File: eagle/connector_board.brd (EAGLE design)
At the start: 22.6 x 24.3 mm, 26 parts, among them IC1 MEGA8-MI, J1 FH12-6S-0.5SH(55), J2 FH12-6S-0.5SH(55), J3 FH12-6S-0.5SH(55), J4 FH12-6S-0.5SH(55), X4 POGOPIN-CONNWITHVIAS-SMV, X6 POGOPIN-CONNWITHVIAS-SMV

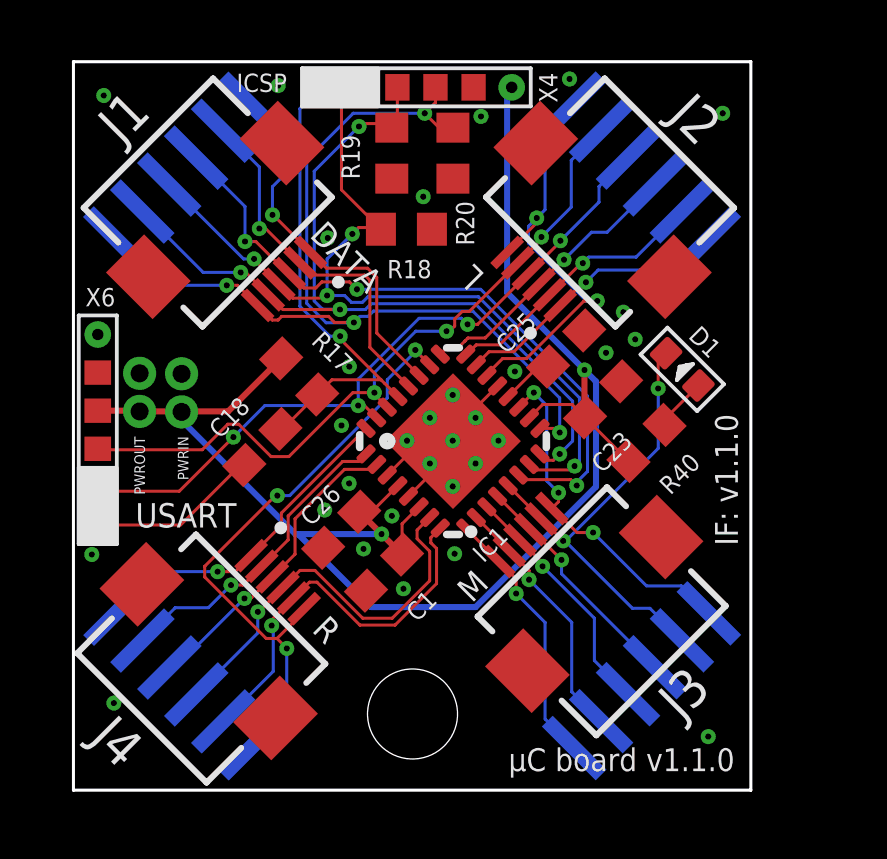
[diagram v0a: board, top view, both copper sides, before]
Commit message: Add pogoprog pads on both sides of board
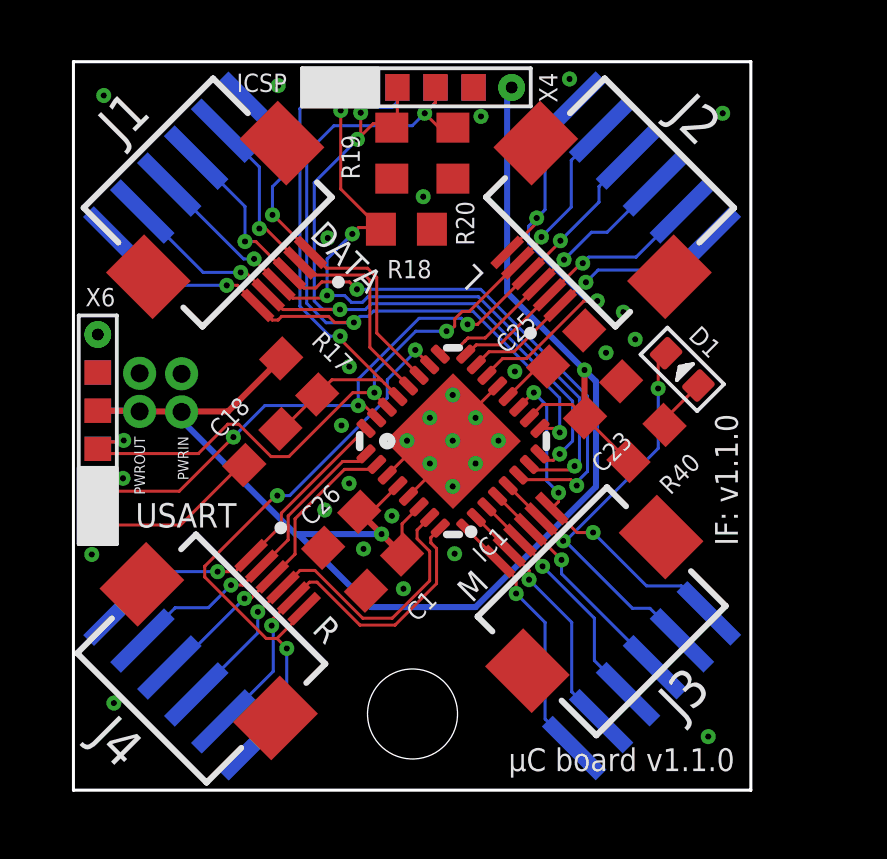
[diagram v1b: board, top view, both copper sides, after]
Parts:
- added X1, X2: POGOPIN-CONNWITHVIAS-SMV, Protofusion:POGOPROG-CONN-OH-SMALLERVIAS
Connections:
- net !RESET: now also X2.1
- net DTR: now also X1.1
- net GND: now also X1.5, X1.6, X2.5
- net MISO: now also X2.3
- net MOSI: now also X2.2
- net RXD: now also X1.3
- net SCK: now also X2.4
- net TXD: now also X1.2
- net VCC: now also X1.4, X2.6
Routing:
- net MISO: track 30.5 -> 33.1 mm, vias 4 -> 5
- net RXD: track 0.12 -> 2.35 mm, vias 0 -> 1
- net TXD: track 0.09 -> 2.10 mm, vias 0 -> 1
- net VCC: track 53.9 -> 55.3 mm
- net SCK: track 32.8 -> 33.9 mm
- net MOSI: track 29.8 -> 30.8 mm, vias 4 -> 5

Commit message: Make room for v-score on the edges by rotating connectors 45degs
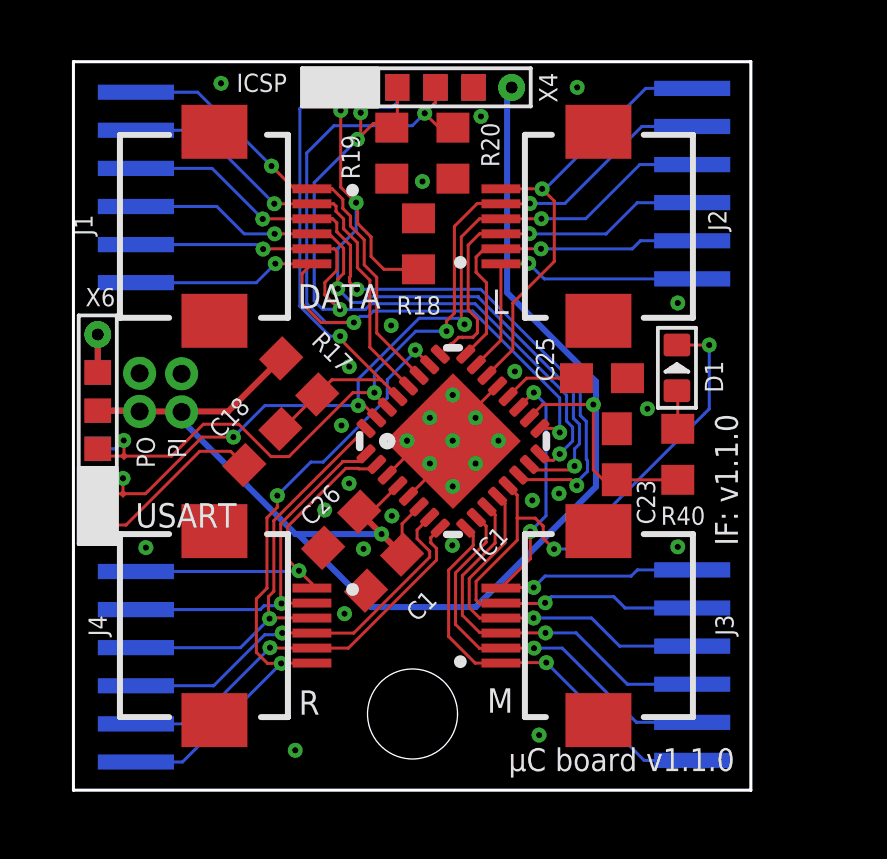
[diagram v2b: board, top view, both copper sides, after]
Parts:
- moved U$3 3.97 mm to (20.6, 23.4), turned to 270 degrees
- moved U$2 3.84 mm to (2.08, 0.94), turned to 90 degrees
- moved J3 3.13 mm to (14.2, 5.49), turned to 90 degrees
- moved J2 2.07 mm to (14.2, 18.8), turned to 90 degrees
- moved J1 1.98 mm to (7.95, 18.8), turned to 270 degrees
- moved C23 1.89 mm to (18.1, 11.2), turned to 90 degrees
- moved J4 1.84 mm to (7.95, 5.49), turned to 270 degrees
- moved U$4 1.63 mm to (2.08, 16.9), turned to 90 degrees
- moved C25 1.55 mm to (17.6, 13.7), turned to 0 degrees
- moved U$1 1.55 mm to (20.6, 7.34), turned to 270 degrees
- moved R40 1.11 mm to (20.1, 11.2), turned to 90 degrees
- moved SH1 0.80 mm to (1.68, 11.1)
- moved SH2 0.79 mm to (1.65, 9.88)
- moved R18 0.63 mm to (11.5, 18.2), turned to 90 degrees
- moved D1 0.18 mm to (20.1, 14.1), turned to 90 degrees
- renumbered PWRIN to PI, PWROUT to PO
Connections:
- net ENCR1A: now also IC1.2; no longer IC1.32
- net LEDR: now also IC1.32; no longer IC1.2
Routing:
- net ENCM2B: track 15.7 -> 24.2 mm, vias 2 -> 3
- net ENCM1A: track 8.83 -> 14.0 mm
- net LEDM: track 8.19 -> 13.1 mm
- net ENCM1B: track 8.51 -> 13.4 mm
- net ENCM2A: track 7.89 -> 12.3 mm
- net MOSI: track 30.8 -> 34.9 mm
- net LEDR: track 10.4 -> 14.0 mm
- net SWM: track 11.7 -> 15.0 mm
- net LEDL: track 9.50 -> 12.6 mm
- net ENCL2B: track 24.3 -> 27.4 mm
- net SDA: track 12.5 -> 15.3 mm
- net ENCL2A: track 24.0 -> 26.8 mm
- net GND: track 4.17 -> 6.71 mm
- net SCL: track 12.2 -> 14.7 mm
- net ENCL1B: track 9.13 -> 11.1 mm
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
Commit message: Fix connector board issues for manufacuring;
The minimum trace width and clearance allowed on a 1.6mm thick pcb is
6mils. For some reason 4mils was used when designing the board (maybe
JLCPCB design rules?).

Also some of the texts were on the wrong layers / places and would not
be printed on the board / would be printed on top of components / other
texts.
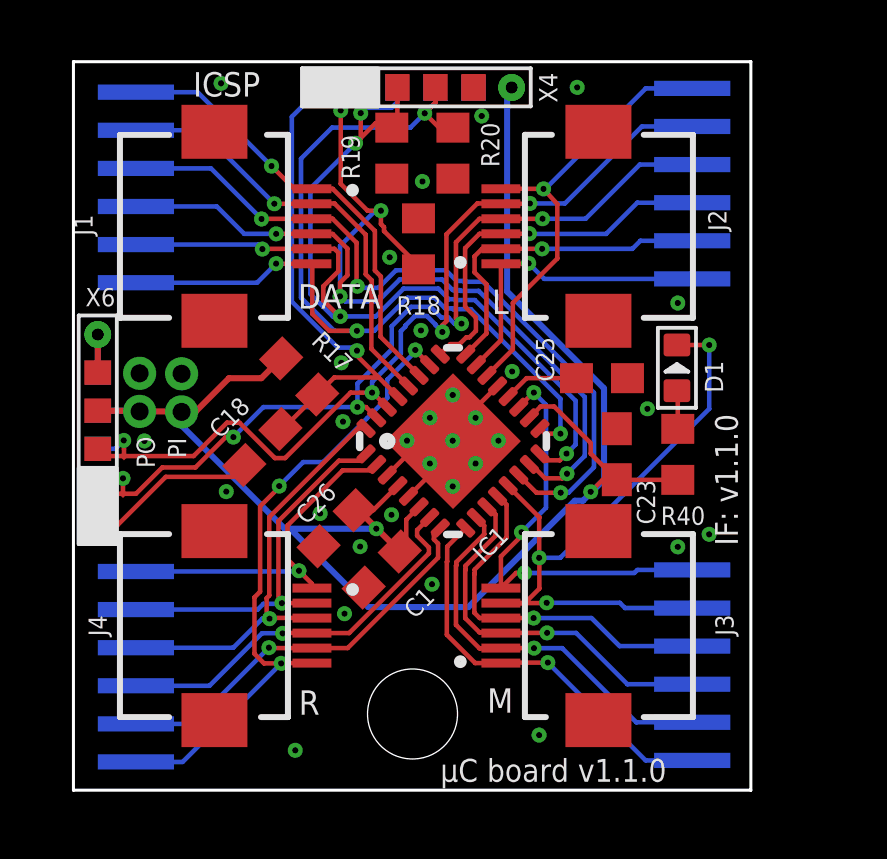
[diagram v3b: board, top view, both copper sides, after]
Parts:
- moved C26 0.16 mm to (8.77, 8.73)
- moved C1 0.13 mm to (10.3, 7.35)
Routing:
- net ENCM2B: track 24.2 -> 22.7 mm
- net MISO: track 34.2 -> 35.6 mm
- net MOSI: track 34.9 -> 35.9 mm
- net !SS: track 24.3 -> 25.3 mm
- net ENCL2A: track 26.8 -> 27.7 mm
- net ENCL2B: track 27.4 -> 28.1 mm
- net SCK: track 34.3 -> 34.9 mm

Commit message: Fix manufacturing issues in connector board;
* The design rules used previously were wrong. The minimun trace widht,
clearance and drill size were too small. The correct values are as
follows:
  * Minimum via drill: 0.3mm
  * Minimum trace width: 6mils
  * Minimum clearance: 6mils

* Some smaller fixes were also done e.g. solder mask stop was added
  below the uC, labels were repositioned and moved to the correct layers
  and such.
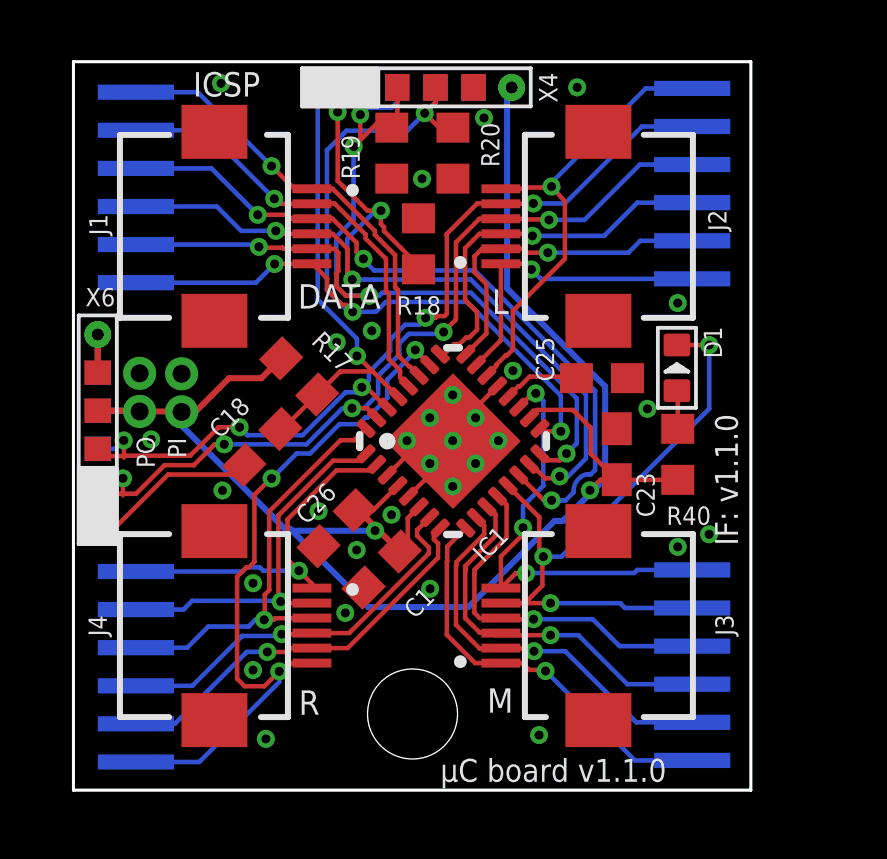
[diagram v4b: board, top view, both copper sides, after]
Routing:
- net SCK: track 34.9 -> 31.4 mm
- net SWR: track 21.6 -> 23.9 mm
- net MISO: track 35.6 -> 33.6 mm
- net MOSI: track 35.9 -> 34.3 mm
- net ENCL2B: track 28.1 -> 26.6 mm, vias 3 -> 4
- net ENCL2A: track 27.7 -> 26.6 mm
- net !RESET: track 16.4 -> 15.3 mm
- net !SS: track 25.3 -> 24.6 mm
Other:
- board text added: "C1"
- board text added: "C18"
- board text added: "C23"
- board text added: "C25"
- board text added: "C26"
- board text added: "D1"
- board text added: "IC1"
- board text added: "J1"
- board text added: "J2"
- board text added: "J3"
- board text added: "J4"
- board text added: "PI"
- board text added: "PO"
- board text added: "R17"
- board text added: "R18"
- board text added: "R19"
- board text added: "R20"
- board text added: "R40"
- board text added: "X1"
- board text added: "X2"
- board text added: "X4"
- board text added: "X6"
